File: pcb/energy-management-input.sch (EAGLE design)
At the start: 72 parts, among them IC4 74HC165N, IC5 74HC165N, J1 WIRE_HOLE-14AWG, J2 WIRE_HOLE-14AWG, J3 WIRE_HOLE-14AWG, J4 WIRE_HOLE-14AWG, U1 DS1307

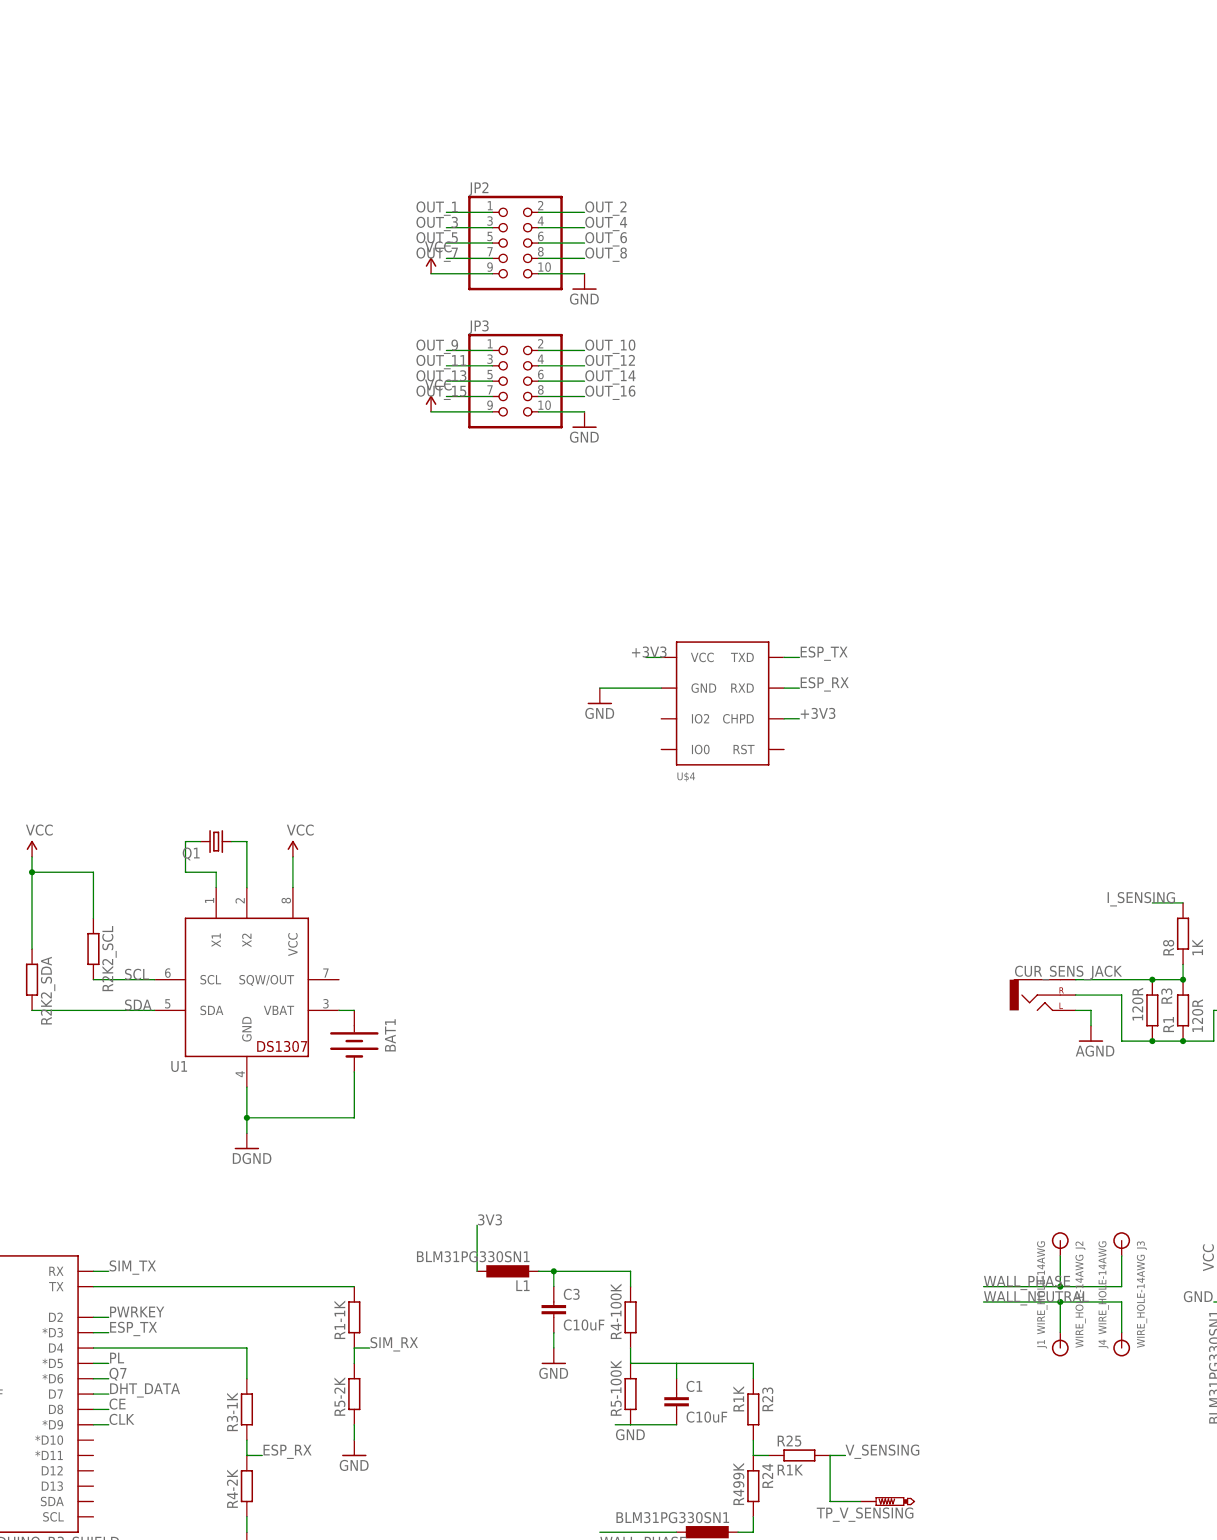
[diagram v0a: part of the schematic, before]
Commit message: Finished Input Board
Input board schematic and routing finished
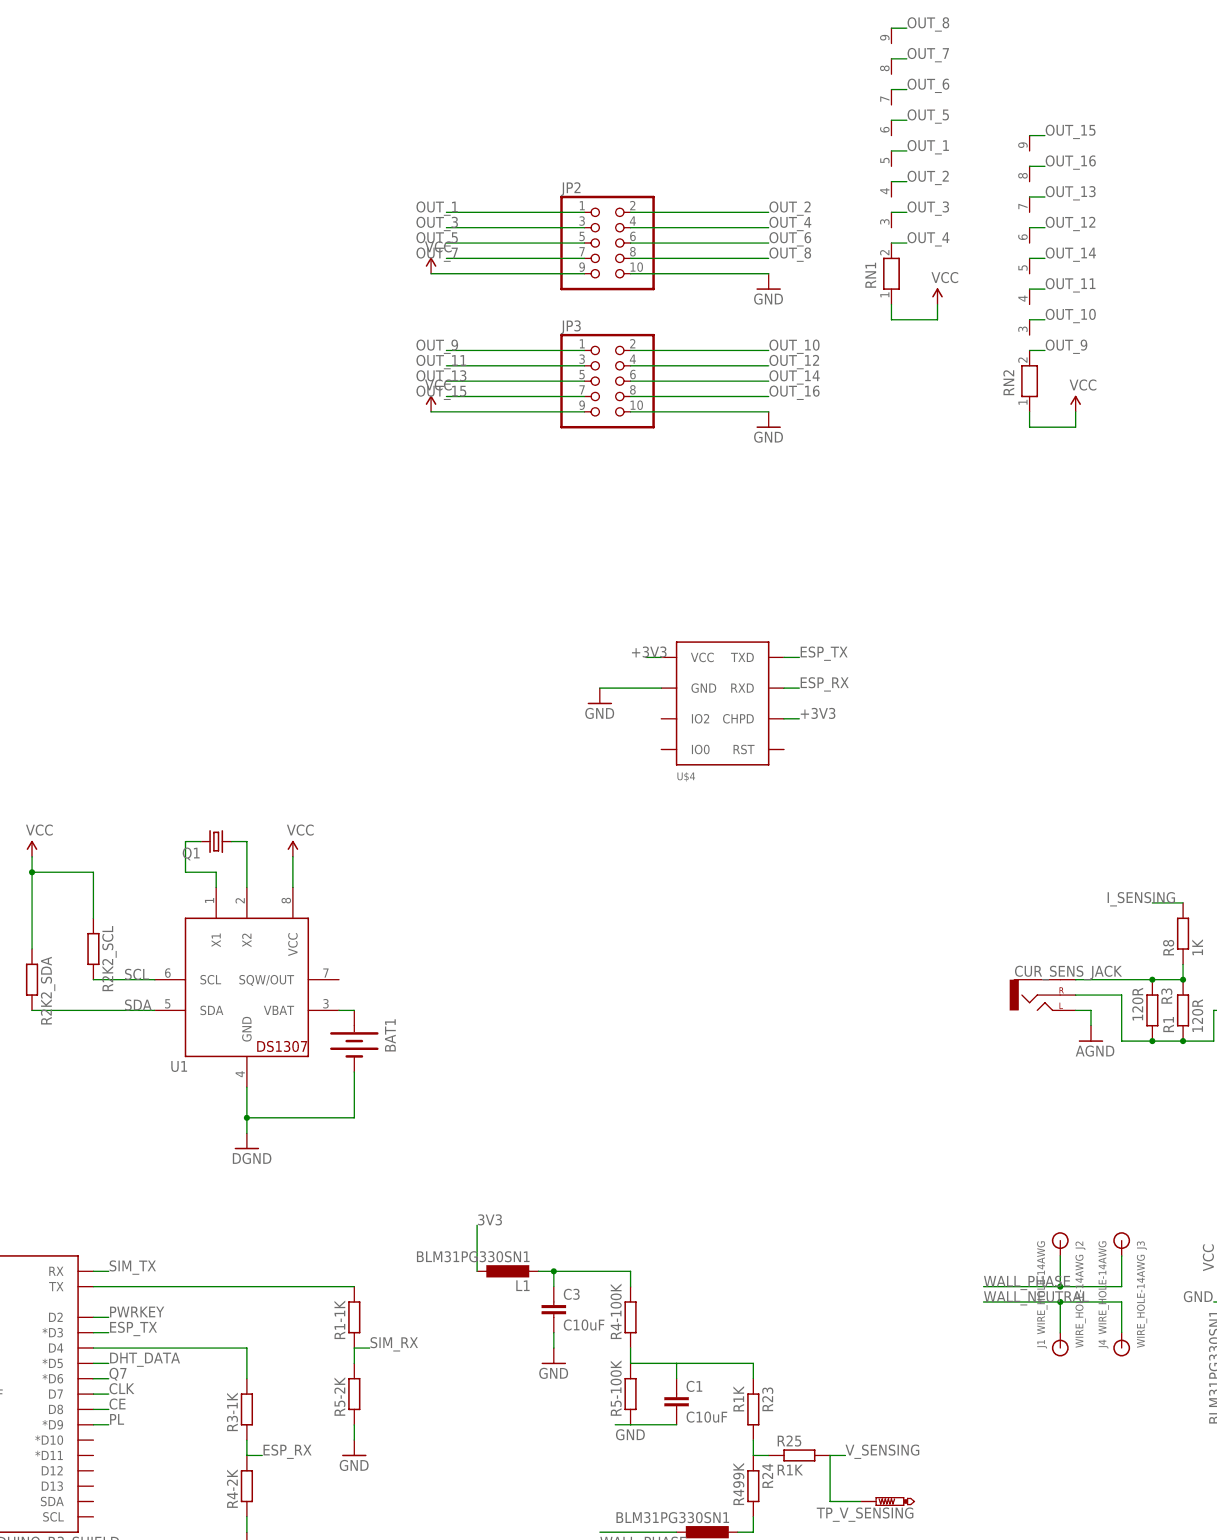
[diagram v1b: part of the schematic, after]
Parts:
- added RN1, RN2: (no value), resistor-net:RN08
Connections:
- net CLK: now also U$1.D7; no longer U$1.*D9
- net DHT_DATA: now also U$1.*D5; no longer U$1.D7
- net OUT_1: now also RN1.5
- net OUT_10: now also RN2.3
- net OUT_11: now also RN2.4
- net OUT_12: now also RN2.6
- net OUT_13: now also RN2.7
- net OUT_14: now also RN2.5
- net OUT_15: now also RN2.9
- net OUT_16: now also RN2.8
- net OUT_2: now also RN1.4
- net OUT_3: now also RN1.3
- net OUT_4: now also RN1.2
- net OUT_5: now also RN1.6
- net OUT_6: now also RN1.7
- net OUT_7: now also RN1.8
- net OUT_8: now also RN1.9
- net OUT_9: now also RN2.2
- net PL: now also U$1.*D9; no longer U$1.*D5
- net VCC: now also RN1.1, RN2.1
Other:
- moved on the sheet: JP2, JP3
